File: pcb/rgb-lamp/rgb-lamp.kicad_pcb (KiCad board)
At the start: 2 copper layers, 12.7 x 40.6 mm, 12 parts, among them J1 HEADER-1x03, U1 WS2812B, U2 WS2812B, U3 WS2812B

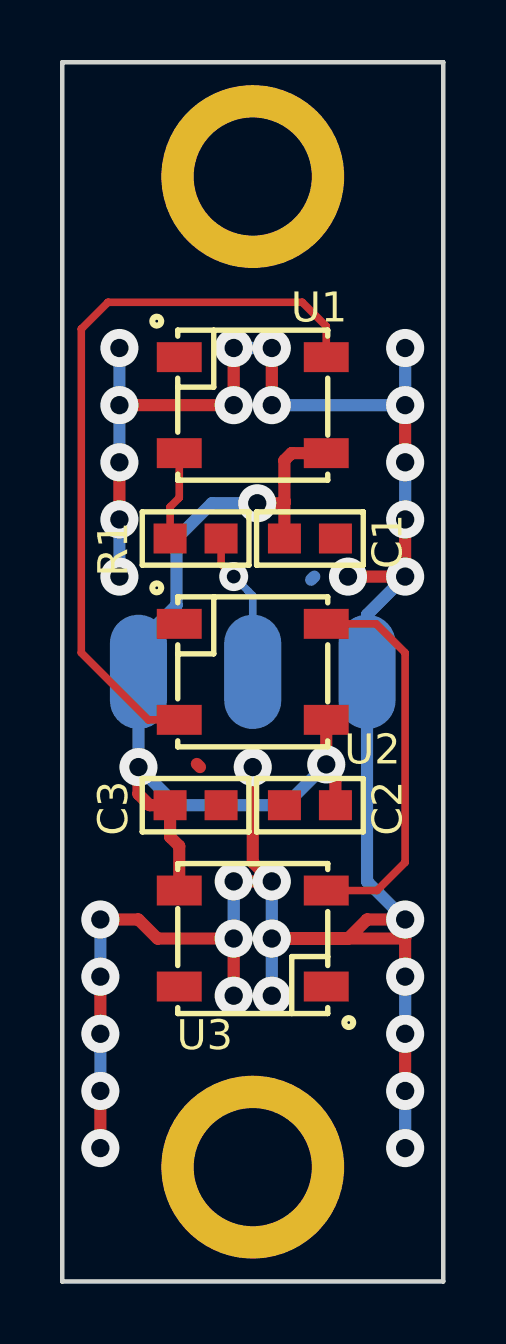
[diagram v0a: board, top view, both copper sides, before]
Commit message: Updated PCB design
+ Completed daughterboard PCB layout.
* Corrected soldermask clerance on front panel pcb.
- Removed input resistor on DIN for RGB lamp board.
* Modified PCB layout for PSU board.
* Updated gerber files.
* Updated schematics pdf, BOM.
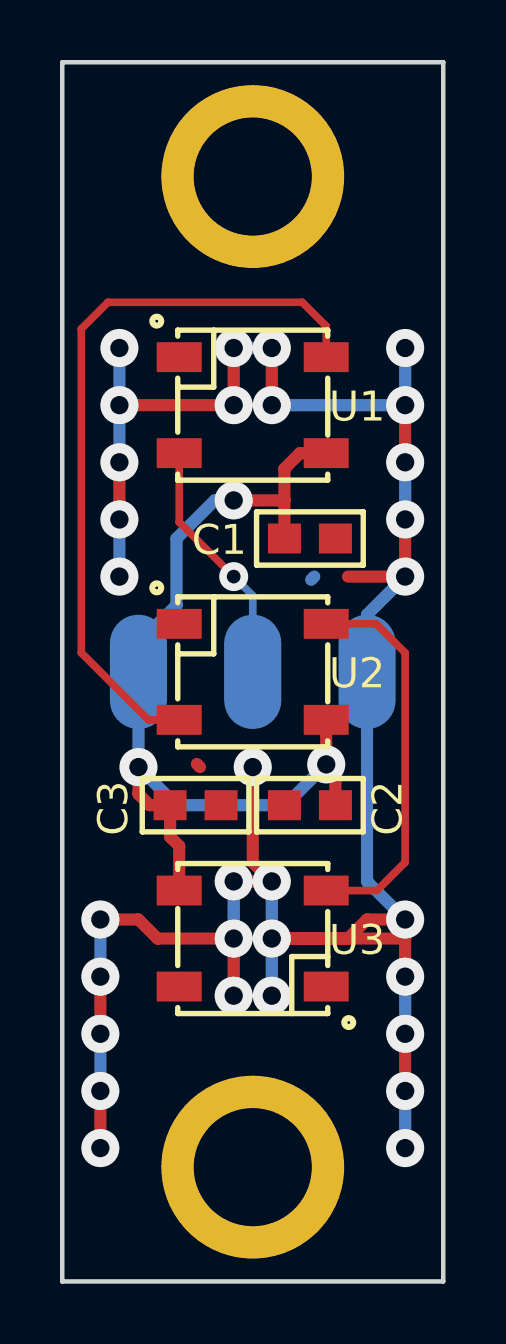
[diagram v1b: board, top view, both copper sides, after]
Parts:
- removed R1: 300, smt:R-0603
- U1, U2, U3: value WS2812B -> IN-PI554FCH
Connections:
- U1 pad 4: Net-(R1-Pad2) -> Net-(J1-Pad2)
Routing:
- net Net-(J1-Pad2): track 4.88 -> 8.30 mm
- net Net-(R1-Pad2): track 2.97 -> 0.00 mm
- net GND: track 86.3 -> 86.4 mm, vias 32 -> 31
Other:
- board text added: "REV. B"
- board text removed: "REV. A"
